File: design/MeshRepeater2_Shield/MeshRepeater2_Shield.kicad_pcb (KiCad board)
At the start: 2 copper layers, 90 x 60 mm, 6 parts

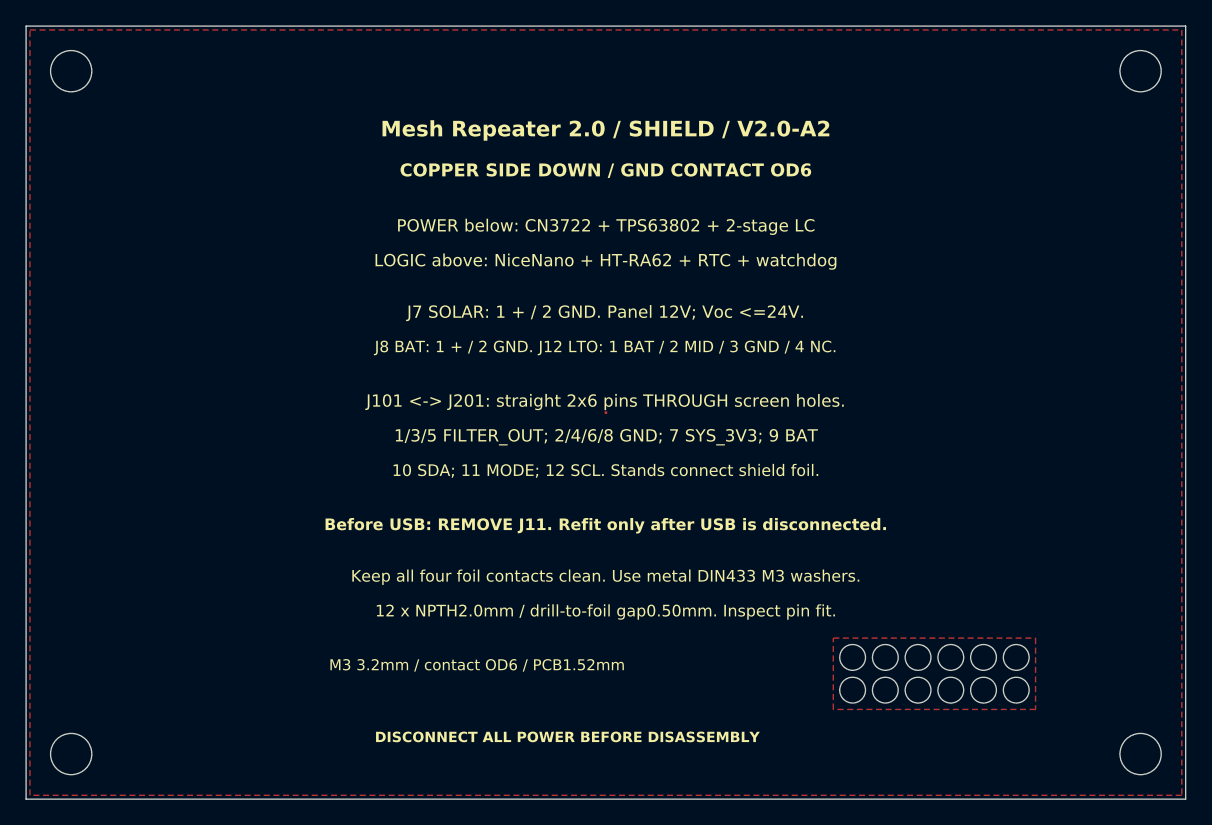
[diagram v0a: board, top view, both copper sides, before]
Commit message: Publish Mesh Repeater 2.0 A3 prototype and engineering audit
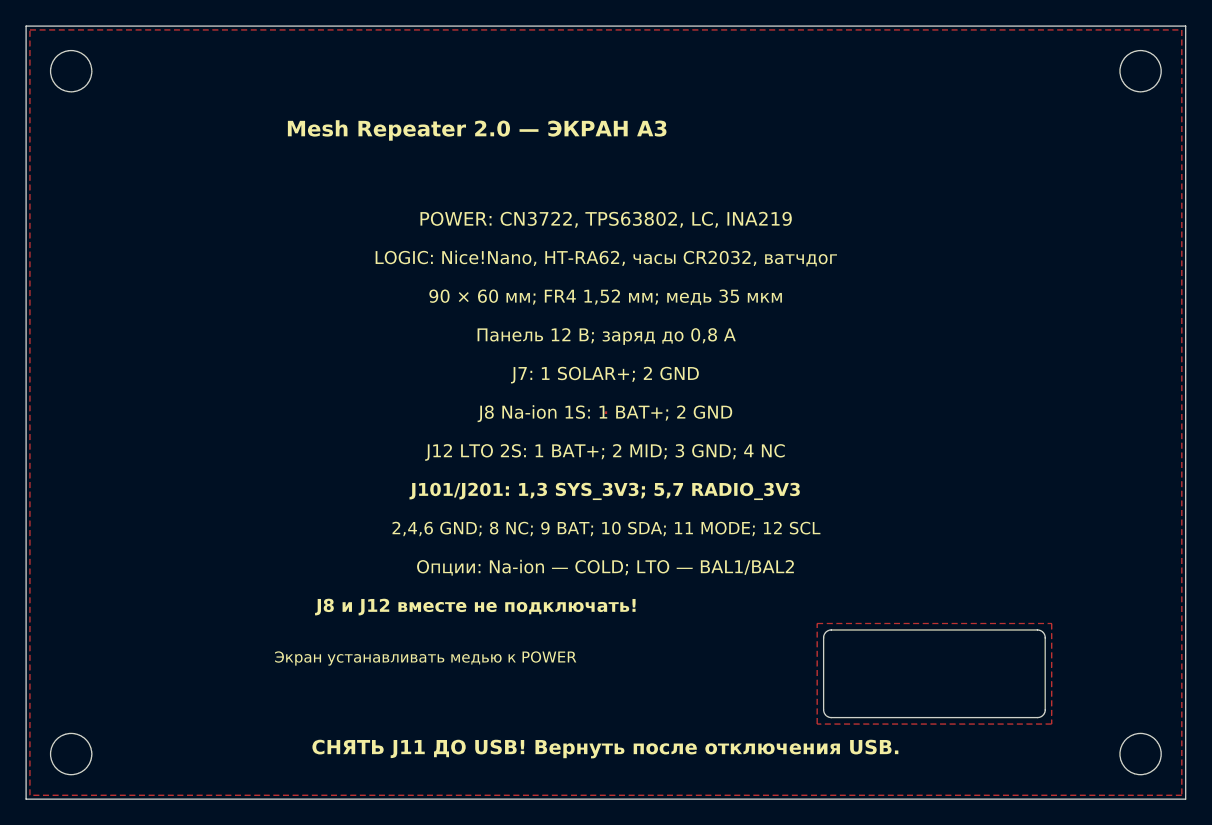
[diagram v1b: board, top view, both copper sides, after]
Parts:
- HS1: value INTERCONNECT PASS-THROUGH -> ОКНО МЕЖПЛАТНОГО РАЗЪЁМА; footprint Shield:Shield_Interconnect_2x06_NPTH_D2_CuVoid3 -> Shield:Shield_Interconnect_Window17p2x6p8_R0p6
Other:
- board text added: "2,4,6 GND; 8 NC; 9 BAT; 10 SDA; 11 MODE; 12 SCL"
- board text added: "90 × 60 мм; FR4 1,52 мм; медь 35 мкм"
- board text added: "J101/J201: 1,3 SYS_3V3; 5,7 RADIO_3V3"
- board text added: "J12 LTO 2S: 1 BAT+; 2 MID; 3 GND; 4 NC"
- board text added: "J7: 1 SOLAR+; 2 GND"
- board text added: "J8 Na-ion 1S: 1 BAT+; 2 GND"
- board text added: "J8 и J12 вместе не подключать!"
- board text added: "LOGIC: Nice!Nano, HT-RA62, часы CR2032, ватчдог"
- board text added: "Mesh Repeater 2.0 — ЭКРАН A3"
- board text added: "POWER: CN3722, TPS63802, LC, INA219"
- board text added: "Опции: Na-ion — COLD; LTO — BAL1/BAL2"
- board text added: "Панель 12 В; заряд до 0,8 А"
- board text added: "СНЯТЬ J11 ДО USB! Вернуть после отключения USB."
- board text added: "Экран устанавливать медью к POWER"
- board text removed: "1/3/5 FILTER_OUT; 2/4/6/8 GND; 7 SYS_3V3; 9 BAT"
- board text removed: "10 SDA; 11 MODE; 12 SCL. Stands connect shield foil."
- board text removed: "12 x NPTH2.0mm / drill-to-foil gap0.50mm. Inspect pin fit."
- board text removed: "Before USB: REMOVE J11. Refit only after USB is disconnected."
- board text removed: "Below: stand 18mm + washer. Above: washer + stand 15mm."
- board text removed: "COPPER SIDE DOWN / GND CONTACT OD6"
- board text removed: "DISCONNECT ALL POWER BEFORE DISASSEMBLY"
- board text removed: "GPS: J4 Heltec T114 pinout; power enable nRF P0.24."
- board text removed: "J101 <-> J201: straight 2x6 pins THROUGH screen holes."
- board text removed: "J7 SOLAR: 1 + / 2 GND. Panel 12V; Voc <=24V."
- board text removed: "J8 BAT: 1 + / 2 GND. J12 LTO: 1 BAT / 2 MID / 3 GND / 4 NC."
- board text removed: "Keep all four foil contacts clean. Use metal DIN433 M3 washers."
- board text removed: "LOGIC above: NiceNano + HT-RA62 + RTC + watchdog"
- board text removed: "LTO 2S: fit BAL1/BAL2; omit COLD. R56 0R"
- board text removed: "M3 3.2mm / contact OD6 / PCB1.52mm"
- board text removed: "Mesh Repeater 2.0 / SHIELD / V2.0-A2"
- board text removed: "Metal washers DIN433 3.2 x 6 x 0.5mm; 5 per corner."
- board text removed: "Na-ion 1S: fit COLD; omit BAL1/BAL2. R56 1.8R"
- board text removed: "Na-ion without COLD: omit cold parts; R56 0R"
- board text removed: "POWER below: CN3722 + TPS63802 + 2-stage LC"
- board text removed: "Pin35mm / socket8.5mm / nominal engagement4.48mm."
- board text removed: "R15 130k R16 49.9k"
- board text removed: "R15 40.2k R16 49.9k"
- board text removed: "R3 121k R4 100k C30 6.8pF"
- board text removed: "R3 61.9k R4 100k C30 12pF"
- board text removed: "RTC: CR2032 primary cell. D3 CHARGE / D4 DONE on POWER."
- board text removed: "UPPER FACE / ASSEMBLY QUICK GUIDE"
- board text removed: "USB / firmware: REMOVE J11. ISP J10 is on LOGIC."

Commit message: Publish A5 routing fixes and CC BY-NC-SA licensing
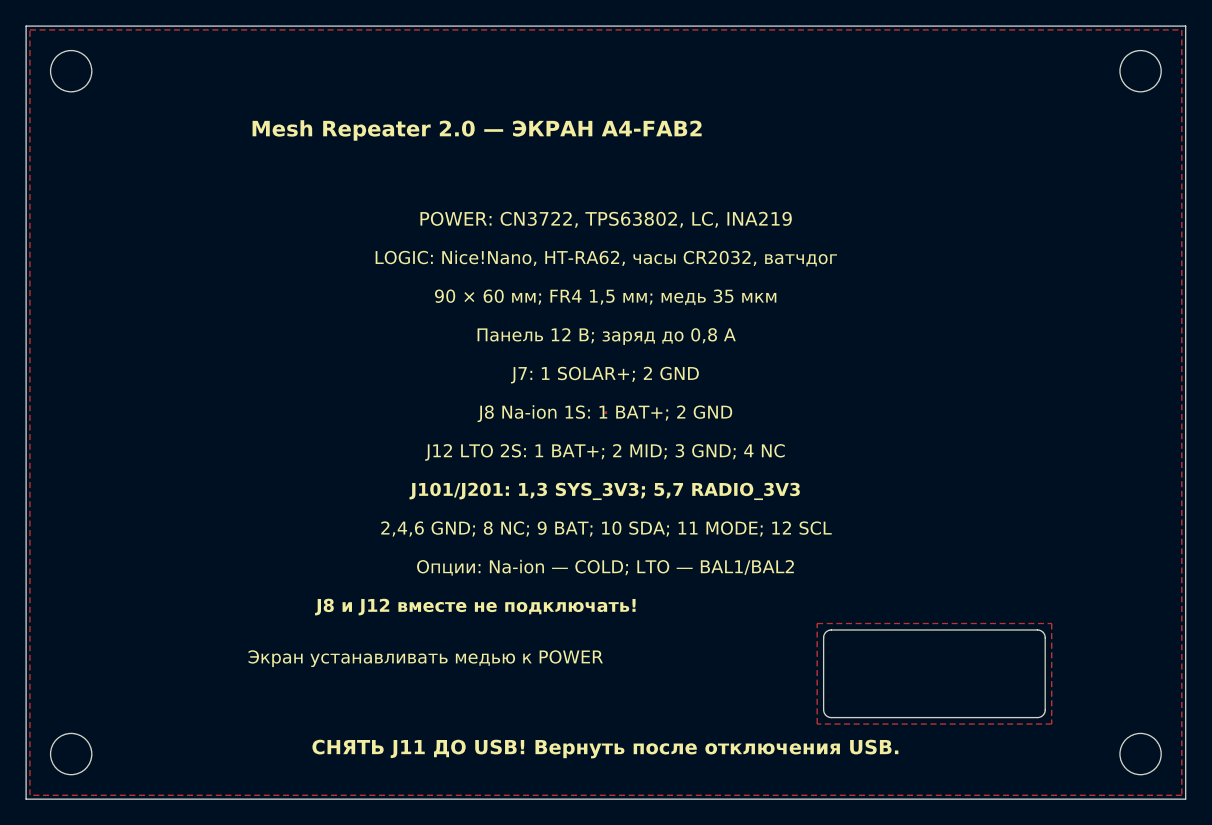
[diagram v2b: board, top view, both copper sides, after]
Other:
- board text added: "90 × 60 мм; FR4 1,5 мм; медь 35 мкм"
- board text added: "Mesh Repeater 2.0 — ЭКРАН A4-FAB2"
- board text removed: "90 × 60 мм; FR4 1,52 мм; медь 35 мкм"
- board text removed: "Mesh Repeater 2.0 — ЭКРАН A3"
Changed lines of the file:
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@@
 	(title_block
 		(title "Mesh Repeater 2.0 / средний экран")
-		(date "2026-10-13")
-		(rev "V2.0-A3")
+		(date "2026-10-16")
+		(rev "V2.0-A4-FAB2")
 		(company "Designed by @Alksndritm")
 	)
@@
 		(effects
 			(font
-				(size 0.85 0.85)
-				(thickness 0.13)
+				(size 1 1)
+				(thickness 0.15)
 			)
 		)
@@
 		(effects
 			(font
-				(size 0.95 0.95)
-				(thickness 0.13)
+				(size 1 1)
+				(thickness 0.15)
 			)
 		)
@@
 			(font
 				(size 1 1)
-				(thickness 0.13)
-			)
-		)
-	)
-	(gr_text "90 × 60 мм; FR4 1,52 мм; медь 35 мкм"
+				(thickness 0.15)
+			)
+		)
+	)
+	(gr_text "90 × 60 мм; FR4 1,5 мм; медь 35 мкм"
 		(at 45 21 0)
 		(layer "F.SilkS")
@@
 			(font
 				(size 1 1)
-				(thickness 0.13)
+				(thickness 0.15)
 			)
 		)
@@
 			(font
 				(size 1 1)
-				(thickness 0.13)
+				(thickness 0.15)
 			)
 		)
@@
 			(font
 				(size 1 1)
-				(thickness 0.13)
+				(thickness 0.15)
 			)
 		)
@@
 			(font
 				(size 1 1)
-				(thickness 0.13)
+				(thickness 0.15)
 			)
 		)
@@
 			(font
 				(size 1 1)
-				(thickness 0.13)
+				(thickness 0.15)
 			)
 		)
@@
 			(font
 				(size 1 1)
-				(thickness 0.13)
+				(thickness 0.15)
 			)
 		)
@@
 			(font
 				(size 1.05 1.05)
-				(thickness 0.13)
+				(thickness 0.15)
 			)
 		)
@@
 		)
 	)
-	(gr_text "Mesh Repeater 2.0 — ЭКРАН A3"
+	(gr_text "Mesh Repeater 2.0 — ЭКРАН A4-FAB2"
 		(at 35 8 0)
 		(layer "F.SilkS")
@@
 		(effects
 			(font
-				(size 0.85 0.85)
-				(thickness 0.13)
+				(size 1 1)
+				(thickness 0.15)
 			)
 			(justify mirror)
@@
 		(effects
 			(font
-				(size 0.95 0.95)
-				(thickness 0.13)
+				(size 1 1)
+				(thickness 0.15)
 			)
 			(justify mirror)
@@
 			(font
 				(size 1 1)
-				(thickness 0.13)
+				(thickness 0.15)
 			)
 			(justify mirror)
@@
 			(font
 				(size 1 1)
-				(thickness 0.13)
+				(thickness 0.15)
 			)
 			(justify mirror)
@@
 			(font
 				(size 1 1)
-				(thickness 0.13)
+				(thickness 0.15)
 			)
 			(justify mirror)
@@
 			(font
 				(size 1 1)
-				(thickness 0.13)
+				(thickness 0.15)
 			)
 			(justify mirror)
@@
 			(font
 				(size 1 1)
-				(thickness 0.13)
-			)
-			(justify mirror)
-		)
-	)
-	(gr_text "90 × 60 мм; FR4 1,52 мм; медь 35 мкм"
+				(thickness 0.15)
+			)
+			(justify mirror)
+		)
+	)
+	(gr_text "90 × 60 мм; FR4 1,5 мм; медь 35 мкм"
 		(at 45 39 180)
 		(layer "B.SilkS")
@@
 			(font
 				(size 1 1)
-				(thickness 0.13)
+				(thickness 0.15)
 			)
 			(justify mirror)
@@
 			(font
 				(size 1 1)
-				(thickness 0.13)
+				(thickness 0.15)
 			)
 			(justify mirror)
@@
 			(font
 				(size 1.05 1.05)
-				(thickness 0.13)
+				(thickness 0.15)
 			)
 			(justify mirror)
@@
 		)
 	)
-	(gr_text "Mesh Repeater 2.0 — ЭКРАН A3"
+	(gr_text "Mesh Repeater 2.0 — ЭКРАН A4-FAB2"
 		(at 35 52 180)
 		(layer "B.SilkS")
